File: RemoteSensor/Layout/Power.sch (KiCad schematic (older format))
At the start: 22 parts, among them J1 USB_B_Micro, J2 BATT_CONN, Q1 2N7002, U1 MCP73831-2-OT, U2 LM3671MF, U3 BD48ExxG, U4 BD48ExxG, U5 LM3671MF

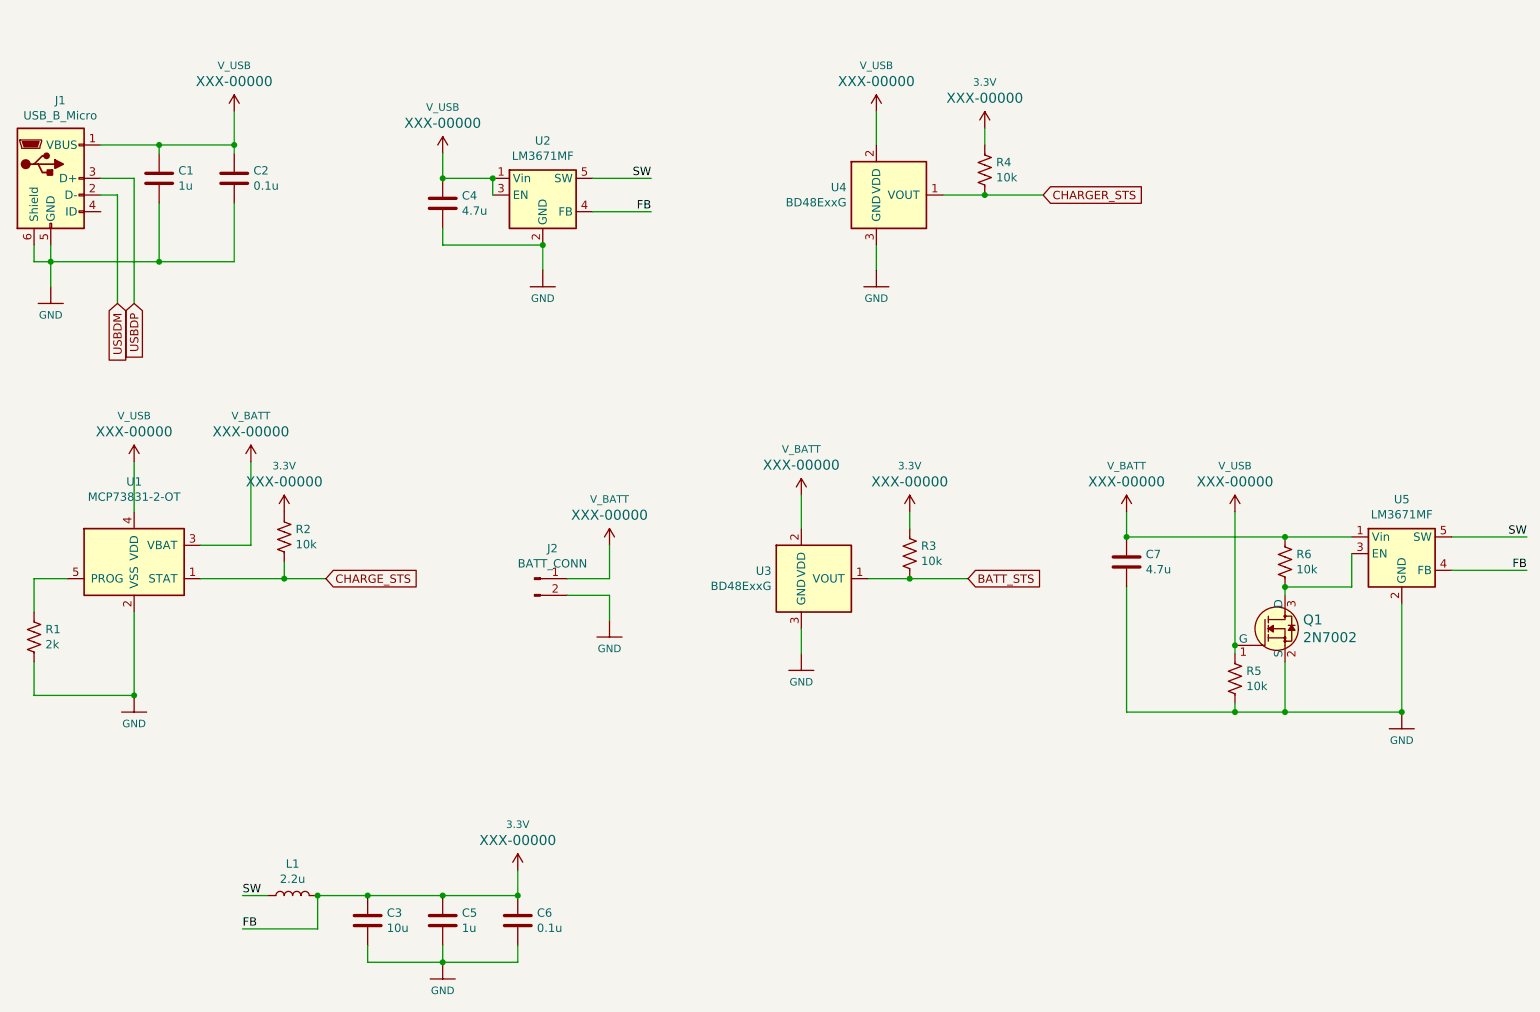
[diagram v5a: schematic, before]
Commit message: Change the USB switching regulator for an LDO
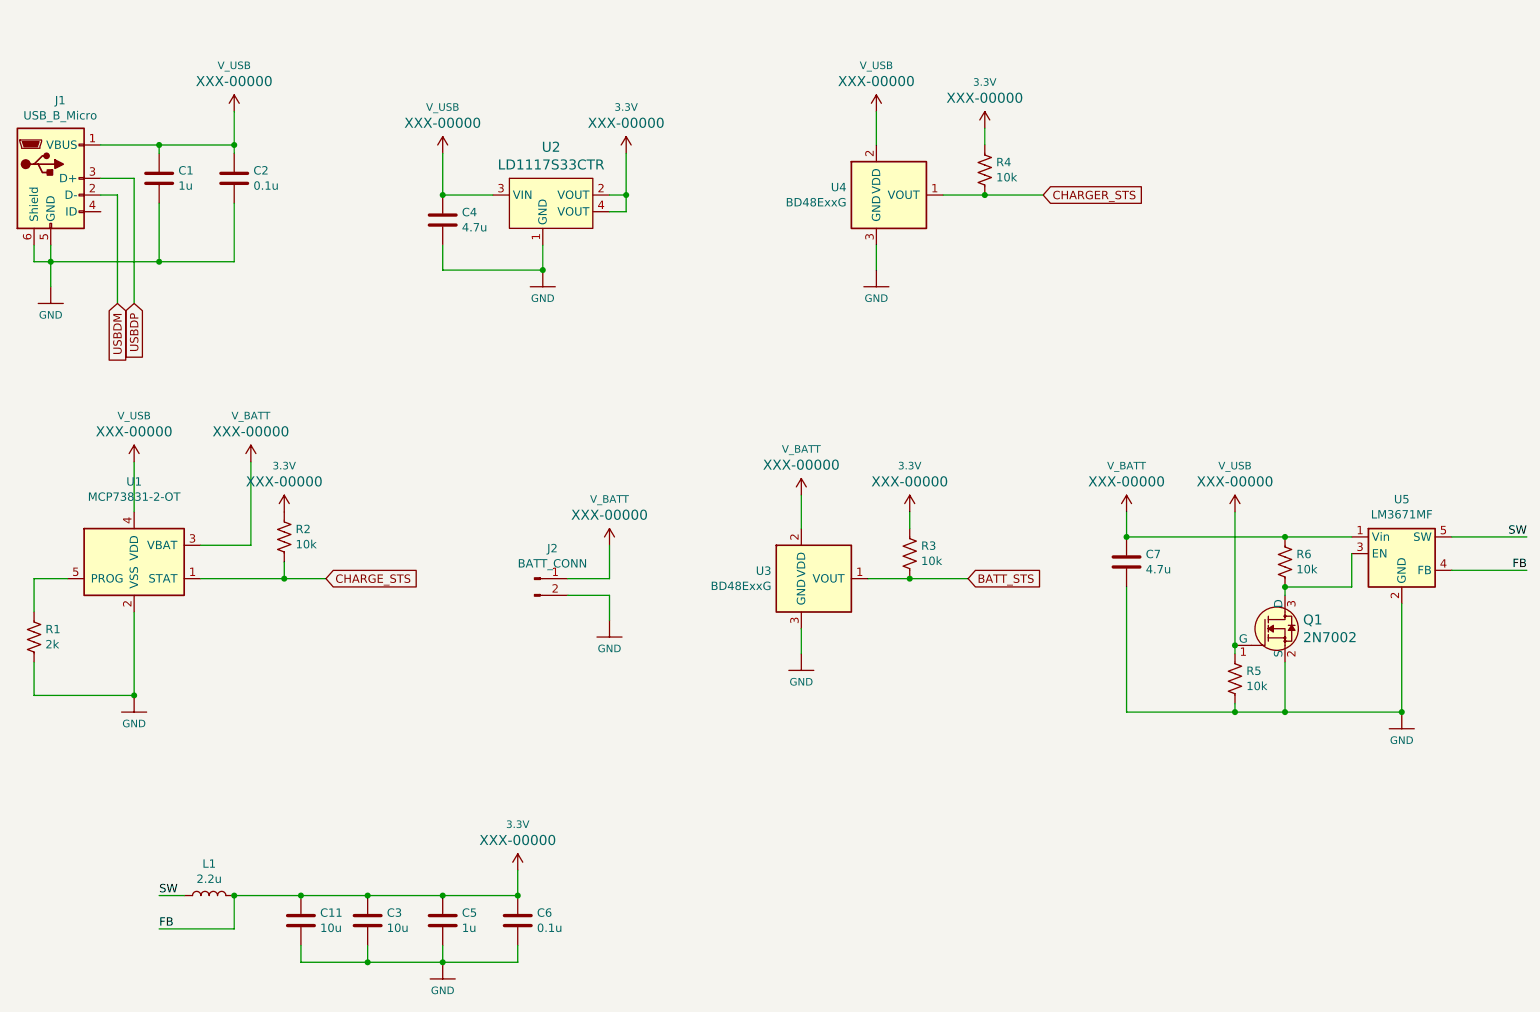
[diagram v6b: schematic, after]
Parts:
- removed U2: LM3671MF, Package_TO_SOT_SMD:TSOT-23-5, symbol Regulator_Switching:LM3670MF
- added C11: 10u, Capacitor_SMD:C_0603_1608Metric_Pad1.05x0.95mm_HandSolder, symbol Device:C
- added U2: LD1117S33CTR, digikey-footprints:SOT-223, symbol dk_PMIC-Voltage-Regulators-Linear:LD1117S33CTR
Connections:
- net 3.3V: now also C11.1, U2.2 (VOUT), U2.4 (VOUT)
- net GND: now also C11.2, U2.1 (GND)
- net V_USB: now also U2.3 (VIN)
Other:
- moved on the sheet: C4, L1
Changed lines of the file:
@@
 	4900 4500 4900 4650
-$Comp
-L Regulator_Switching:LM3670MF U?
-U 1 1 5EEC2141
-P 4500 2100
-AR Path="/5EEC2141" Ref="U?"  Part="1"
-AR Path="/5EE9FD3C/5EEC2141" Ref="U2"  Part="1"
-F 0 "U2" H 4500 2425 50  0000 C CNN
-F 1 "LM3671MF" H 4500 2334 50  0000 C CNN
-F 2 "Package_TO_SOT_SMD:TSOT-23-5" H 4550 1850 50  0001 L CNN
-F 3 "http://www.ti.com/lit/ds/symlink/lm3670.pdf" H 4250 1750 50  0001 C CNN
-	1    4500 2100
-	1    0    0    -1
-$EndComp
-Wire Wire Line
-	4200 2100 4200 2000
 $Comp
 L Device:L L?
 U 1 1 5EEC2148
-P 3000 6300
+P 2500 6300
 AR Path="/5EEC2148" Ref="L?"  Part="1"
 AR Path="/5EE9FD3C/5EEC2148" Ref="L1"  Part="1"
-F 0 "L1" V 3190 6300 50  0000 C CNN
-F 1 "2.2u" V 3099 6300 50  0000 C CNN
-F 2 "Inductor_SMD:L_Taiyo-Yuden_NR-24xx_HandSoldering" H 3000 6300 50  0001 C CNN
-F 3 "~" H 3000 6300 50  0001 C CNN
-	1    3000 6300
+F 0 "L1" V 2690 6300 50  0000 C CNN
+F 1 "2.2u" V 2599 6300 50  0000 C CNN
+F 2 "Inductor_SMD:L_Taiyo-Yuden_NR-24xx_HandSoldering" H 2500 6300 50  0001 C CNN
+F 3 "~" H 2500 6300 50  0001 C CNN
+	1    2500 6300
 	0    -1   -1   0
 $EndComp
 Wire Wire Line
-	3150 6300 3150 6500
-Wire Wire Line
-	3150 6500 2700 6500
+	2650 6300 2650 6500
+Wire Wire Line
+	2650 6500 2200 6500
 $Comp
 L Device:C C?
 U 1 1 5EEC2151
-P 3900 2150
+P 3900 2250
 AR Path="/5EEC2151" Ref="C?"  Part="1"
 AR Path="/5EE9FD3C/5EEC2151" Ref="C4"  Part="1"
-F 0 "C4" H 4015 2196 50  0000 L CNN
-F 1 "4.7u" H 4015 2105 50  0000 L CNN
-F 2 "Capacitor_SMD:C_0603_1608Metric_Pad1.05x0.95mm_HandSolder" H 3938 2000 50  0001 C CNN
-F 3 "~" H 3900 2150 50  0001 C CNN
-	1    3900 2150
-	1    0    0    -1
-$EndComp
-Wire Wire Line
-	3900 2300 3900 2400
-Wire Wire Line
-	3900 2400 4500 2400
-Wire Wire Line
-	3900 2000 4200 2000
-Connection ~ 3900 2000
-Connection ~ 4200 2000
+F 0 "C4" H 4015 2296 50  0000 L CNN
+F 1 "4.7u" H 4015 2205 50  0000 L CNN
+F 2 "Capacitor_SMD:C_0603_1608Metric_Pad1.05x0.95mm_HandSolder" H 3938 2100 50  0001 C CNN
+F 3 "~" H 3900 2250 50  0001 C CNN
+	1    3900 2250
+	1    0    0    -1
+$EndComp
 $Comp
 L Device:C C?
@@
 	1    0    0    -1
 $EndComp
-Wire Wire Line
-	3150 6300 3450 6300
-Connection ~ 3150 6300
+Connection ~ 2650 6300
 Wire Wire Line
 	3450 6300 3900 6300
-Connection ~ 3450 6300
 Wire Wire Line
 	3450 6700 3450 6600
-Connection ~ 4500 2400
 Wire Wire Line
 	3450 6700 3900 6700
@@
 $EndComp
 Wire Wire Line
-	3900 1850 3900 2000
-Wire Wire Line
 	4350 6150 4350 6300
 Connection ~ 3900 6300
@@
 $EndComp
 Wire Wire Line
-	4800 2000 5150 2000
-Wire Wire Line
-	4800 2200 5150 2200
-Wire Wire Line
 	9950 4150 10400 4150
 Wire Wire Line
 	9950 4350 10400 4350
-Text Label 5150 2000 2    50   ~ 0
-SW
-Text Label 5150 2200 2    50   ~ 0
-FB
 Text Label 10400 4150 2    50   ~ 0
 SW
@@
 FB
 Wire Wire Line
-	2850 6300 2700 6300
-Text Label 2700 6300 0    50   ~ 0
+	2350 6300 2200 6300
+Text Label 2200 6300 0    50   ~ 0
 SW
-Text Label 2700 6500 0    50   ~ 0
+Text Label 2200 6500 0    50   ~ 0
 FB
 Text GLabel 3200 4400 2    50   Input ~ 0
@@
 Text GLabel 1950 2750 3    50   Input ~ 0
 USBDM
+$Comp
+L dk_PMIC-Voltage-Regulators-Linear:LD1117S33CTR U2
+U 1 1 5F145B16
+P 4500 2100
+F 0 "U2" H 4550 2387 60  0000 C CNN
+F 1 "LD1117S33CTR" H 4550 2281 60  0000 C CNN
+F 2 "digikey-footprints:SOT-223" H 4700 2300 60  0001 L CNN
+F 3 "http://www.st.com/content/ccc/resource/technical/document/datasheet/99/3b/7d/91/91/51/4b/be/CD00000544.pdf/files/CD00000544.pdf/jcr:content/translations/en.CD00000544.pdf" H 4700 2400 60  0001 L CNN
+F 4 "497-1241-1-ND" H 4700 2500 60  0001 L CNN "Digi-Key_PN"
+F 5 "LD1117S33CTR" H 4700 2600 60  0001 L CNN "MPN"
+F 6 "Integrated Circuits (ICs)" H 4700 2700 60  0001 L CNN "Category"
+F 7 "PMIC - Voltage Regulators - Linear" H 4700 2800 60  0001 L CNN "Family"
+F 8 "http://www.st.com/content/ccc/resource/technical/document/datasheet/99/3b/7d/91/91/51/4b/be/CD00000544.pdf/files/CD00000544.pdf/jcr:content/translations/en.CD00000544.pdf" H 4700 2900 60  0001 L CNN "DK_Datasheet_Link"
+F 9 "/product-detail/en/stmicroelectronics/LD1117S33CTR/497-1241-1-ND/586241" H 4700 3000 60  0001 L CNN "DK_Detail_Page"
+F 10 "IC REG LINEAR 3.3V 800MA SOT223" H 4700 3100 60  0001 L CNN "Description"
+F 11 "STMicroelectronics" H 4700 3200 60  0001 L CNN "Manufacturer"
+F 12 "Active" H 4700 3300 60  0001 L CNN "Status"
+	1    4500 2100
+	1    0    0    -1
+$EndComp
+Wire Wire Line
+	3900 1850 3900 2100
+Wire Wire Line
+	3900 2100 4200 2100
+Connection ~ 3900 2100
+Wire Wire Line
+	3900 2400 3900 2550
+Wire Wire Line
+	3900 2550 4500 2550
+Connection ~ 4500 2550
+Wire Wire Line
+	4900 2100 5000 2100
+Wire Wire Line
+	5000 2100 5000 2200
+Wire Wire Line
+	5000 2200 4900 2200
+$Comp
+L SparkFun-PowerSymbols:3.3V #SUPPLY0123
+U 1 1 5F2F9BC4
+P 5000 1850
+F 0 "#SUPPLY0123" H 5050 1850 45  0001 L BNN
+F 1 "3.3V" H 5000 2126 45  0000 C CNN
+F 2 "XXX-00000" H 5000 2031 60  0000 C CNN
+F 3 "" H 5000 1850 60  0001 C CNN
+	1    5000 1850
+	1    0    0    -1
+$EndComp
+Wire Wire Line
+	5000 1850 5000 2100
+Connection ~ 5000 2100
+$Comp
+L Device:C C?
+U 1 1 5F2FE4BE
+P 3050 6450
+AR Path="/5F2FE4BE" Ref="C?"  Part="1"
+AR Path="/5EE9FD3C/5F2FE4BE" Ref="C11"  Part="1"
+F 0 "C11" H 3165 6496 50  0000 L CNN
+F 1 "10u" H 3165 6405 50  0000 L CNN
+F 2 "Capacitor_SMD:C_0603_1608Metric_Pad1.05x0.95mm_HandSolder" H 3088 6300 50  0001 C CNN
+F 3 "~" H 3050 6450 50  0001 C CNN
+	1    3050 6450
+	1    0    0    -1
+$EndComp
+Wire Wire Line
+	2650 6300 3050 6300
+Wire Wire Line
+	3050 6300 3450 6300
+Connection ~ 3050 6300
+Connection ~ 3450 6300
+Wire Wire Line
+	3050 6600 3050 6700
+Wire Wire Line
+	3050 6700 3450 6700
+Connection ~ 3450 6700
 $EndSCHEMATC

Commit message: Change what pins are used for i2c
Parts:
- C1, C11, C2, C3, C4, C5, C6, C7: symbol Device:C -> RemoteSensor-rescue:C-Device
- J1: symbol Connector:USB_B_Micro -> RemoteSensor-rescue:USB_B_Micro-Connector
- J2: symbol Connector:Conn_01x02_Male -> RemoteSensor-rescue:Conn_01x02_Male-Connector
- L1: symbol Device:L -> RemoteSensor-rescue:L-Device
- R1, R2, R3, R4, R5, R6: symbol Device:R_US -> RemoteSensor-rescue:R_US-Device
- U1: symbol Battery_Management:MCP73831-2-OT -> RemoteSensor-rescue:MCP73831-2-OT-Battery_Management
- U2: symbol dk_PMIC-Voltage-Regulators-Linear:LD1117S33CTR -> RemoteSensor-rescue:LD1117S33CTR-dk_PMIC-Voltage-Regulators-Linear
- U3, U4: symbol Power_Management:BD48ExxG -> RemoteSensor-rescue:BD48ExxG-Power_Management
- U5: symbol Regulator_Switching:LM3670MF -> RemoteSensor-rescue:LM3670MF-Regulator_Switching
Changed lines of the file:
@@
 $EndComp
 $Comp
-L Device:C C7
+L RemoteSensor-rescue:C-Device C7
 U 1 1 5EEB1255
 P 8000 4300
@@
 $EndComp
 $Comp
-L Device:R_US R6
+L RemoteSensor-rescue:R_US-Device R6
 U 1 1 5EEB1282
 P 8950 4300
@@
 	8950 4150 9350 4150
 $Comp
-L Device:R_US R5
+L RemoteSensor-rescue:R_US-Device R5
 U 1 1 5EEB12A2
 P 8650 5000
@@
 $EndComp
 $Comp
-L Connector:USB_B_Micro J?
+L RemoteSensor-rescue:USB_B_Micro-Connector J?
 U 1 1 5EEC20C4
 P 1550 2000
@@
 $EndComp
 $Comp
-L Device:C C?
+L RemoteSensor-rescue:C-Device C?
 U 1 1 5EEC20D6
 P 2200 2000
@@
 $EndComp
 $Comp
-L Device:C C?
+L RemoteSensor-rescue:C-Device C?
 U 1 1 5EEC20DC
 P 2650 2000
@@
 Connection ~ 2650 1800
 $Comp
-L Battery_Management:MCP73831-2-OT U?
+L RemoteSensor-rescue:MCP73831-2-OT-Battery_Management U?
 U 1 1 5EEC20F1
 P 2050 4300
@@
 	2050 3700 2050 4000
 $Comp
-L Device:R_US R?
+L RemoteSensor-rescue:R_US-Device R?
 U 1 1 5EEC2106
 P 1450 4750
@@
 Connection ~ 2050 5100
 $Comp
-L Connector:Conn_01x02_Male J?
+L RemoteSensor-rescue:Conn_01x02_Male-Connector J?
 U 1 1 5EEC2118
 P 4450 4400
@@
 $EndComp
 $Comp
-L Device:R_US R?
+L RemoteSensor-rescue:R_US-Device R?
 U 1 1 5EEC2124
 P 2950 4150
@@
 	4900 4500 4900 4650
 $Comp
-L Device:L L?
+L RemoteSensor-rescue:L-Device L?
 U 1 1 5EEC2148
 P 2500 6300
@@
 	2650 6500 2200 6500
 $Comp
-L Device:C C?
+L RemoteSensor-rescue:C-Device C?
 U 1 1 5EEC2151
 P 3900 2250
@@
 $EndComp
 $Comp
-L Device:C C?
+L RemoteSensor-rescue:C-Device C?
 U 1 1 5EEC215C
 P 3450 6450
@@
 $EndComp
 $Comp
-L Device:C C?
+L RemoteSensor-rescue:C-Device C?
 U 1 1 5EEC2162
 P 3900 6450
@@
 	4500 2550 4500 2400
 $Comp
-L Device:C C?
+L RemoteSensor-rescue:C-Device C?
 U 1 1 5EEC2182
 P 4350 6450
@@
 $EndComp
 $Comp
-L Power_Management:BD48ExxG U?
+L RemoteSensor-rescue:BD48ExxG-Power_Management U?
 U 1 1 5EF05E46
 P 6050 4400
@@
 	6050 4850 6050 4700
 $Comp
-L Device:R_US R?
+L RemoteSensor-rescue:R_US-Device R?
 U 1 1 5EF05E53
 P 6700 4250
@@
 	6700 4400 6450 4400
 $Comp
-L Power_Management:BD48ExxG U?
+L RemoteSensor-rescue:BD48ExxG-Power_Management U?
 U 1 1 5EF05E5E
 P 6500 2100
@@
 	6500 2550 6500 2400
 $Comp
-L Device:R_US R?
+L RemoteSensor-rescue:R_US-Device R?
 U 1 1 5EF05E6B
 P 7150 1950
@@
 Connection ~ 8650 4800
 $Comp
-L Regulator_Switching:LM3670MF U5
+L RemoteSensor-rescue:LM3670MF-Regulator_Switching U5
 U 1 1 5EEB129A
 P 9650 4250
@@
 USBDM
 $Comp
-L dk_PMIC-Voltage-Regulators-Linear:LD1117S33CTR U2
+L RemoteSensor-rescue:LD1117S33CTR-dk_PMIC-Voltage-Regulators-Linear U2
 U 1 1 5F145B16
 P 4500 2100
@@
 	5000 2200 4900 2200
 $Comp
-L SparkFun-PowerSymbols:3.3V #SUPPLY0123
+L RemoteSensor-rescue:3.3V-SparkFun-PowerSymbols #SUPPLY0123
 U 1 1 5F2F9BC4
 P 5000 1850
@@
 Connection ~ 5000 2100
 $Comp
-L Device:C C?
+L RemoteSensor-rescue:C-Device C?
 U 1 1 5F2FE4BE
 P 3050 6450

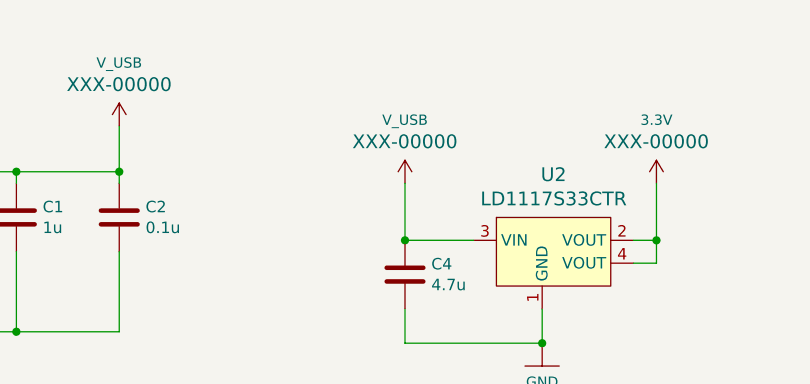
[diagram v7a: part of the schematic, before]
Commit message: Diode protect usb voltage
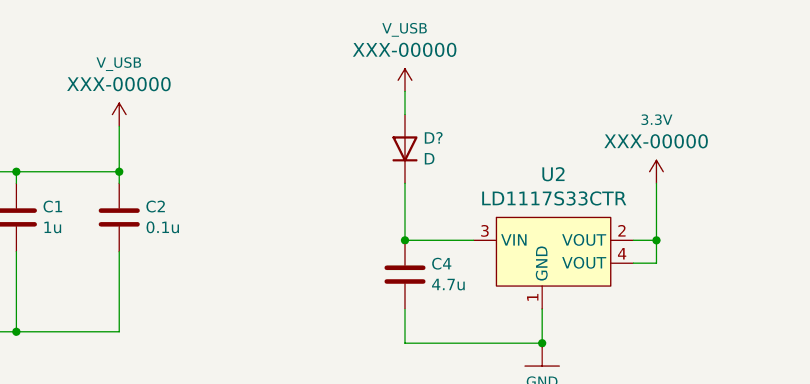
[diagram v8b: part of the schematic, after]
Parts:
- added D?: D, symbol Device:D
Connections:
- net V_USB: now also D?.2 (A); no longer C4.1, U2.3 (VIN)
- new net: C4.1, D?.1 (K), U2.3 (VIN)
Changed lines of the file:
@@
 L RemoteSensor-rescue:V_USB-SparkFun-PowerSymbols #SUPPLY?
 U 1 1 5EEC218D
-P 3900 1850
+P 3900 1450
 AR Path="/5EEC218D" Ref="#SUPPLY?"  Part="1"
 AR Path="/5EE9FD3C/5EEC218D" Ref="#SUPPLY0109"  Part="1"
-F 0 "#SUPPLY0109" H 3950 1850 45  0001 L BNN
-F 1 "V_USB" H 3900 2126 45  0000 C CNN
-F 2 "XXX-00000" H 3900 2031 60  0000 C CNN
-F 3 "" H 3900 1850 60  0001 C CNN
-	1    3900 1850
+F 0 "#SUPPLY0109" H 3950 1450 45  0001 L BNN
+F 1 "V_USB" H 3900 1726 45  0000 C CNN
+F 2 "XXX-00000" H 3900 1631 60  0000 C CNN
+F 3 "" H 3900 1450 60  0001 C CNN
+	1    3900 1450
 	1    0    0    -1
 $EndComp
@@
 	3050 6700 3450 6700
 Connection ~ 3450 6700
+$Comp
+L Device:D D?
+U 1 1 5F56D6D5
+P 3900 1700
+F 0 "D?" V 3946 1620 50  0000 R CNN
+F 1 "D" V 3855 1620 50  0000 R CNN
+F 2 "" H 3900 1700 50  0001 C CNN
+F 3 "~" H 3900 1700 50  0001 C CNN
+	1    3900 1700
+	0    -1   -1   0
+$EndComp
+Wire Wire Line
+	3900 1450 3900 1550
 $EndSCHEMATC
